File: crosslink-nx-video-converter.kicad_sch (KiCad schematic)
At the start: 0 parts

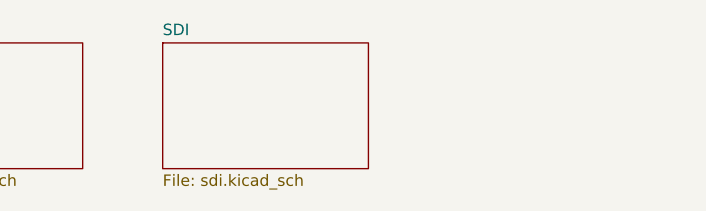
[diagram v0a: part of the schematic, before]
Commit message: Made a connection between DDR3 and fpga on the schematic
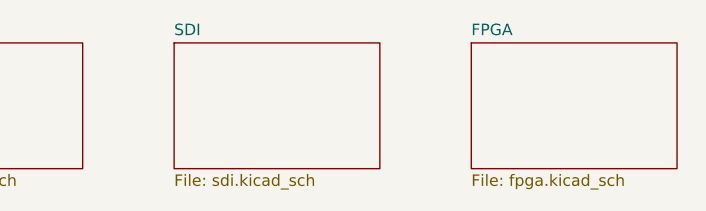
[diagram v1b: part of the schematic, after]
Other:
- added sheet FPGA (fpga.kicad_sch)

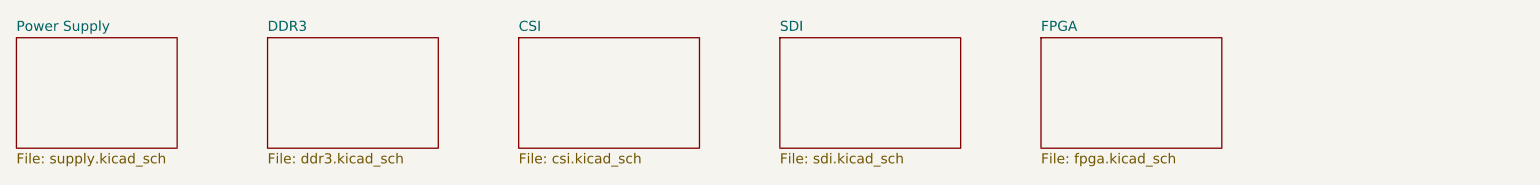
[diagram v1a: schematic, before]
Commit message: Fixed net labels
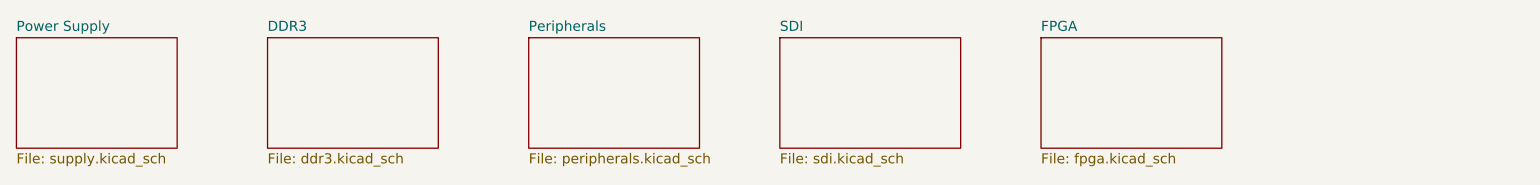
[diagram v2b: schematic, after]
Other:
- removed sheet CSI
- added sheet Peripherals (peripherals.kicad_sch)
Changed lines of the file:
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@@
-    )
-  )
-  (sheet (at 133.35 124.46) (size 22.86 13.97) (fields_autoplaced)
-    (stroke (width 0.1524) (type solid) (color 0 0 0 0))
-    (fill (color 0 0 0 0.0000))
-    (property "Sheet name" "CSI" (id 0) (at 133.35 123.7484 0)
-      (effects (font (size 1.27 1.27)) (justify left bottom))
-    )
-    (property "Sheet file" "csi.kicad_sch" (id 1) (at 133.35 139.0146 0)
-      (effects (font (size 1.27 1.27)) (justify left top))
     )
   )
@@
     )
   )
+  (sheet (at 134.62 124.46) (size 21.59 13.97) (fields_autoplaced)
+    (stroke (width 0.1524) (type solid) (color 0 0 0 0))
+    (fill (color 0 0 0 0.0000))
+    (property "Sheet name" "Peripherals" (id 0) (at 134.62 123.7484 0)
+      (effects (font (size 1.27 1.27)) (justify left bottom))
+    )
+    (property "Sheet file" "peripherals.kicad_sch" (id 1) (at 134.62 139.0146 0)
+      (effects (font (size 1.27 1.27)) (justify left top))
+    )
+  )
   (sheet_instances
     (path "/" (page "1"))
     (path "/818d488b-353f-4d93-a798-315de117413a" (page "2"))
     (path "/ab15e142-a372-4f51-93f5-266aa8f2cc4d" (page "3"))
-    (path "/58a7938d-77ca-4278-af13-189decddc299" (page "4"))
     (path "/754b3b25-858a-4ae9-9c94-eb88092a8c6b" (page "5"))
+    (path "/e402139f-c5ee-4f0d-82a1-944c44608501" (page "6"))
     (path "/921bbf25-96dd-4584-bc75-c5daf08b08e5" (page "6"))
   )
@@
       (reference "#PWR0176") (unit 1) (value "+1V35") (footprint "")
     )
+    (path "/e402139f-c5ee-4f0d-82a1-944c44608501/33196dee-c95d-42c5-9fa8-fa7cc8a81fdc"
+      (reference "#PWR?") (unit 1) (value "GND") (footprint "")
+    )
+    (path "/e402139f-c5ee-4f0d-82a1-944c44608501/7dbab69f-8724-4a1c-b8db-bd192154f5a5"
+      (reference "#PWR?") (unit 1) (value "GND") (footprint "")
+    )
     (path "/818d488b-353f-4d93-a798-315de117413a/5132d7af-0a0a-4920-a030-79e8221755f7"
       (reference "C1") (unit 1) (value "C_1u_0603") (footprint "antmicro-footprints:0603-cap")
@@
       (reference "C45") (unit 1) (value "C_100n_0402") (footprint "antmicro-footprints:0402-cap")
     )
+    (path "/e402139f-c5ee-4f0d-82a1-944c44608501/2728716e-bc32-4049-930e-b6c6d7059021"
+      (reference "J?") (unit 1) (value "WE_68715014522_ONE-SIDE") (footprint "antmicro-footprints:WE_68715014522_ONE-SIDE")
+    )
+    (path "/e402139f-c5ee-4f0d-82a1-944c44608501/c5d0ac94-95d3-491b-bc4e-a20970db84a7"
+      (reference "J?") (unit 1) (value "WE_68715014522") (footprint "antmicro-footprints:WE_68715014522")
+    )
     (path "/818d488b-353f-4d93-a798-315de117413a/37f2baf7-1349-494d-b5e7-a440903a9b98"

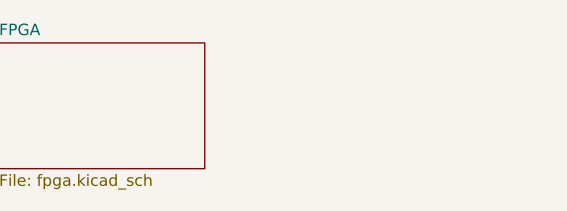
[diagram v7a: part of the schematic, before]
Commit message: Added FPGA configuration circuitry
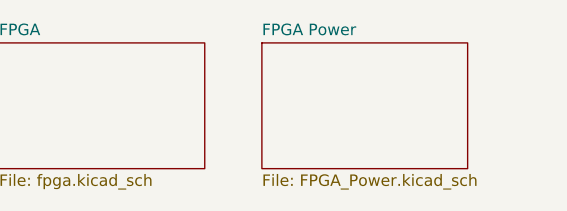
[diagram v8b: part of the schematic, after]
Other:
- added sheet FPGA Power (FPGA_Power.kicad_sch)
